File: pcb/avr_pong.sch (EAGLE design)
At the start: 5 parts, among them U1 ATMEGA328P_PDIP, Y1 16 MHz

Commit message: Updated schematic.
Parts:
- added C3, C4: (no value), rcl:CPOL-USE2.5-5
- added IC1: 7805TV, linear:7805TV
- added ICSP: PINHD-2X3THM, adaprog:PINHD-2X3THM
- added J1: DCJ0202, con-jack:DCJ0202
- added LED1: (no value), led:LED5MM
- added R2: 330, rcl:R-US_0207/10
- added R3, R5: 470, rcl:R-US_0207/10
- added R4: 1k, rcl:R-US_0207/10
- added RIGHT, RIGHT1: TACTILE-SWITCH-PTH, GeekAmmo:TACTILE-SWITCH-PTH
- added RV1: (no value), SparkFun-Electromechanical:POT-RV16AF-20
- added S1: (no value), switch:M251
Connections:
- removed net N$3: R1.2, U1.PC6(/RESET)
- removed net VCC: R1.1, U1.VCC
- new net +5V: C4.+, IC1.VO, ICSP.2, R1.1, R2.1, RV1.A, U1.VCC
- new net MISO: ICSP.1, U1.PB4(MISO)
- new net MOSI: ICSP.4, R5.1, U1.PB3(MOSI/OC2)
- new net N$10: R3.1, U1.PD7(AIN1)
- new net N$11: R4.1, U1.PB1(OC1A)
- new net N$12: R3.2
- new net N$13: R4.2
- new net N$4: LED1.A, R2.2
- new net N$5: C3.+, IC1.VI, J1.1
- new net N$6: J1.2, J1.3
- new net N$7: C3.-, S1.P
- new net N$8: RIGHT1.1, U1.PD2(INT0)
- new net N$9: RV1.S, U1.PC0(ADC0)
- new net RST: ICSP.5, R1.2, RIGHT.3, U1.PC6(/RESET)
- new net SCK: ICSP.3, U1.PB5(SCK)
- net GND: now also C4.-, IC1.GND, ICSP.6, LED1.C, RIGHT.1, RIGHT1.3, RV1.E, S1.O
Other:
- moved on the sheet: R1

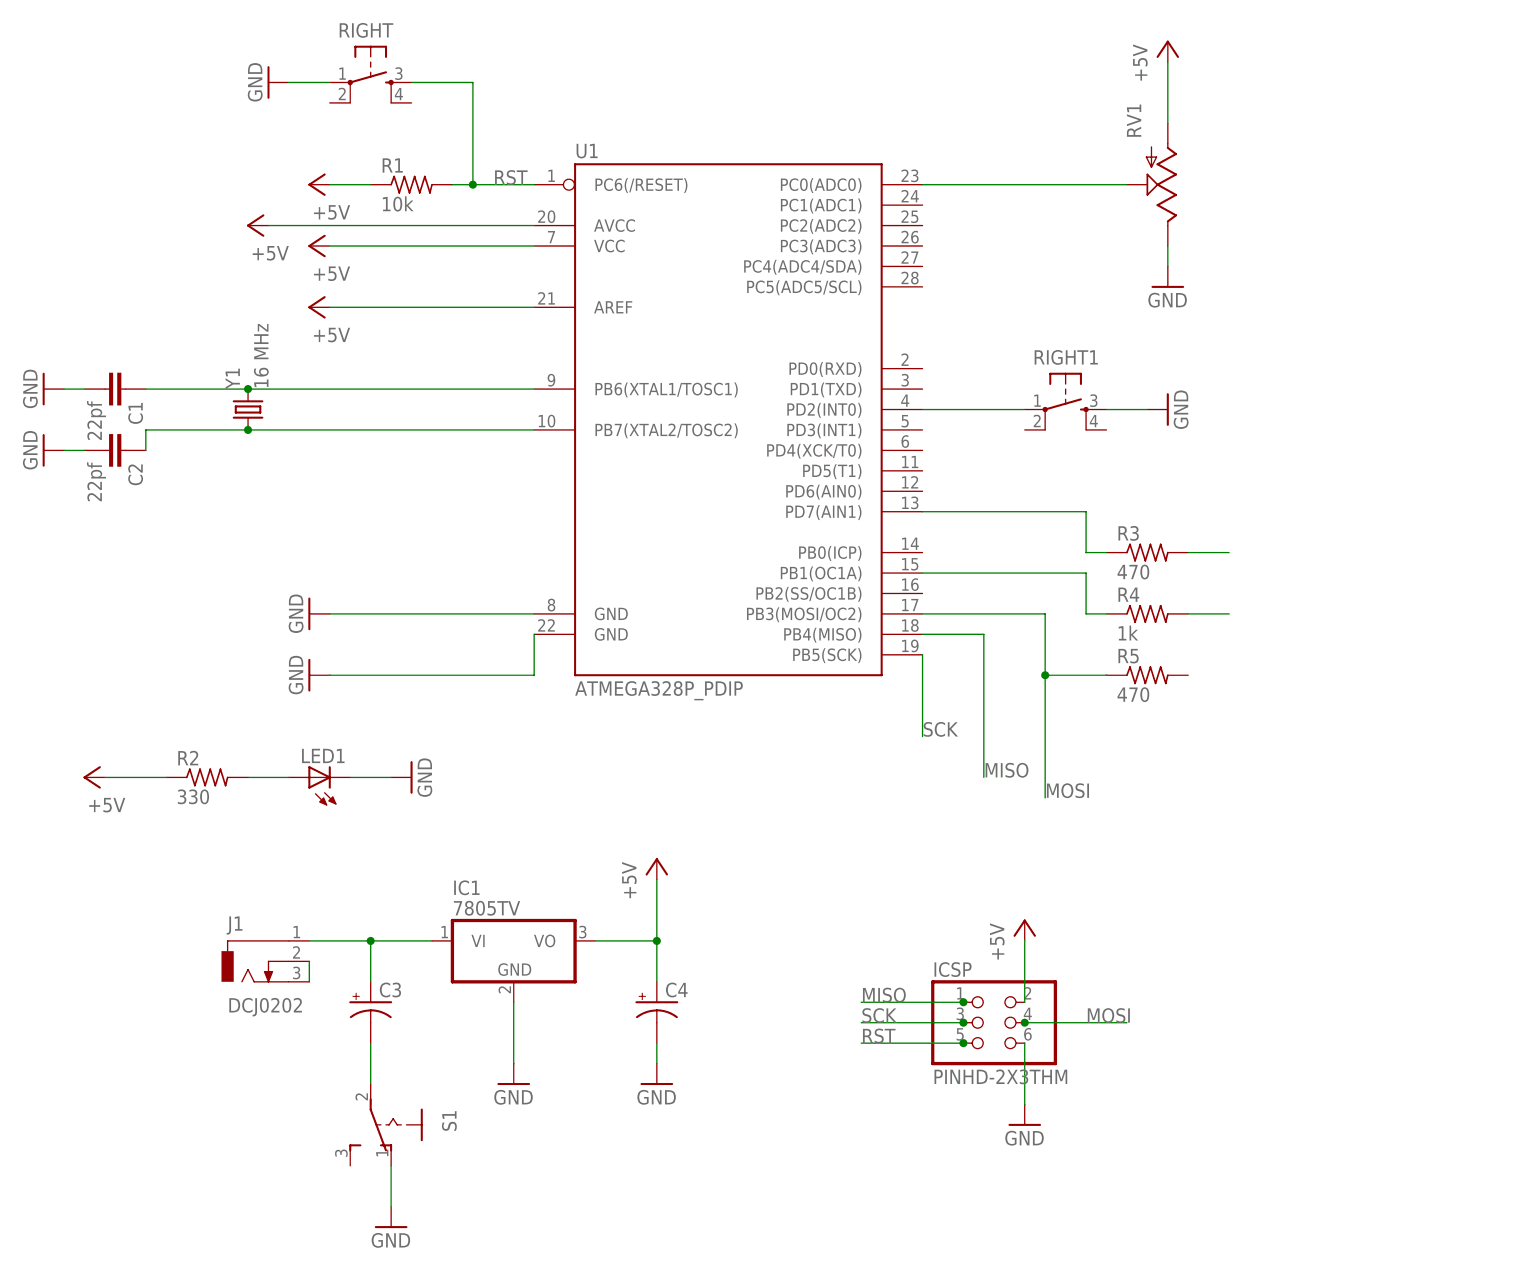
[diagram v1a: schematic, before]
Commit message: Updated schematic and added board layout.
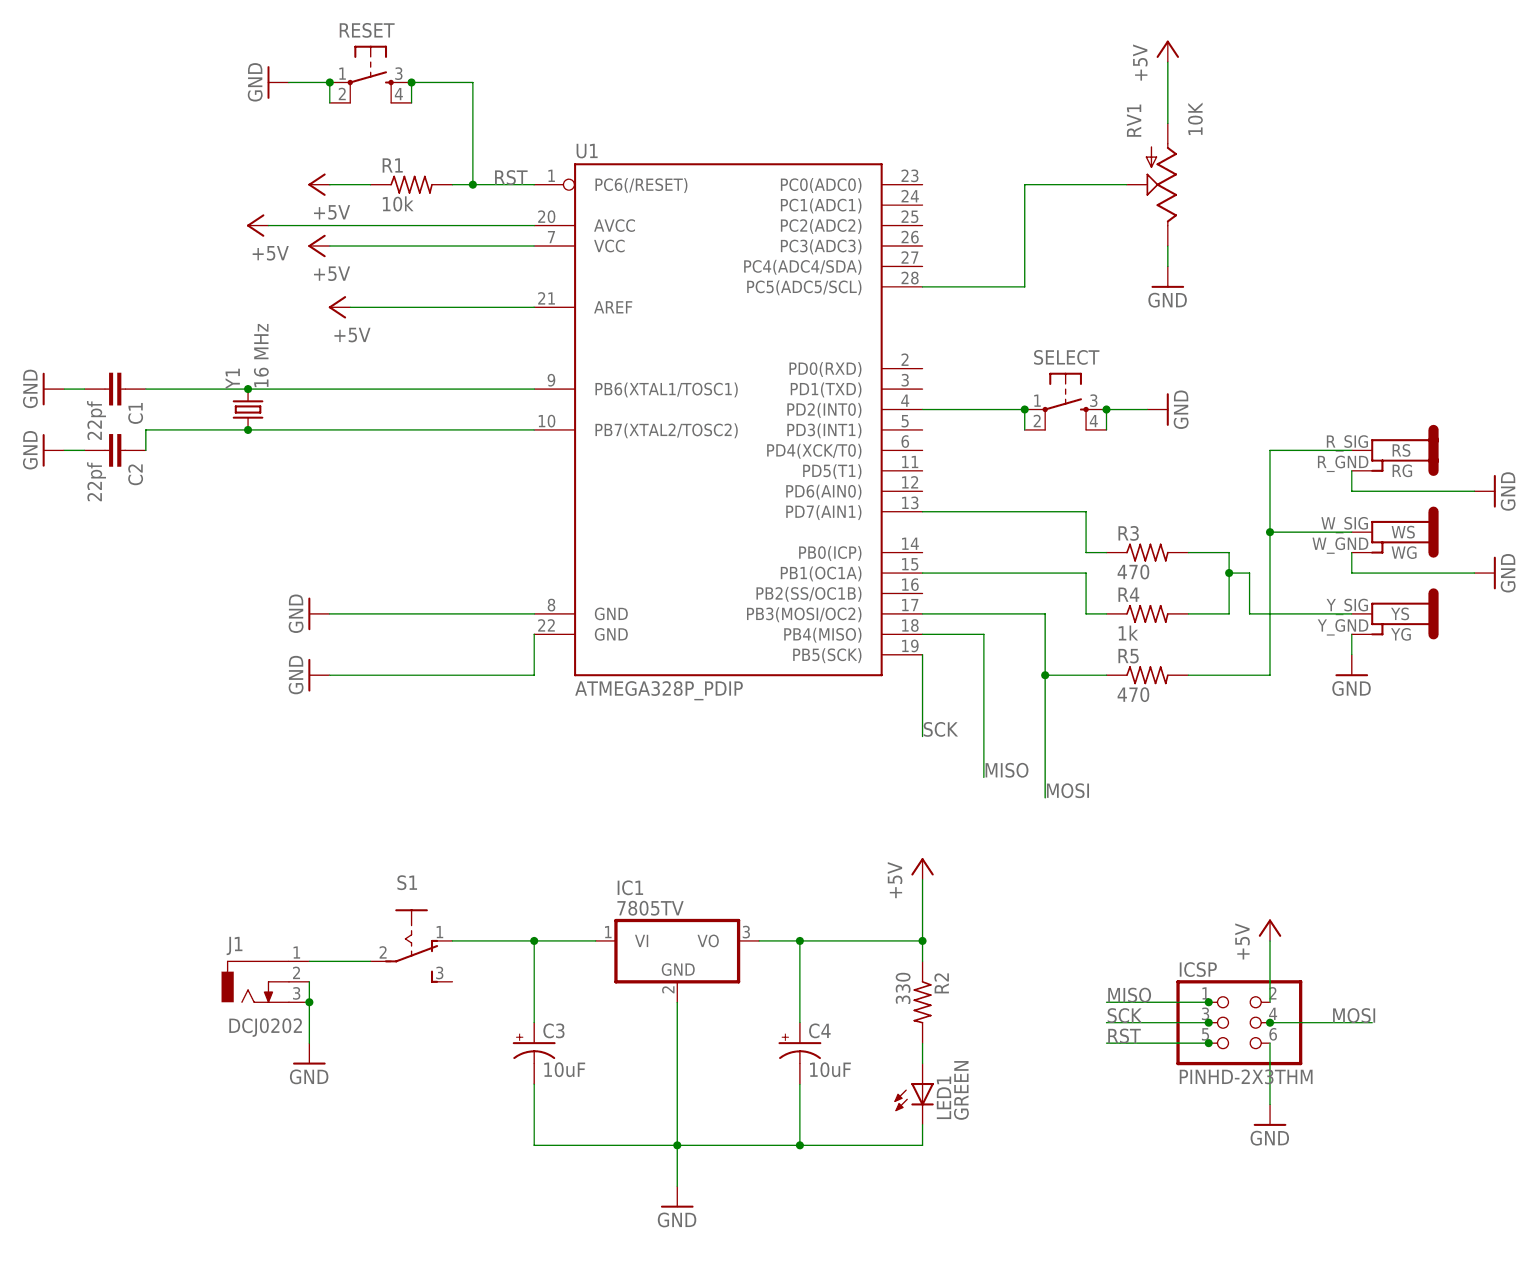
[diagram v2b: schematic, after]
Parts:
- added U$1: 3-RCA-JACK, 3-rca-jack:3-RCA-JACK
- C3, C4: value (none) -> 10uF
- LED1: value (none) -> GREEN
- RV1: value (none) -> 10K
- renumbered RIGHT to RESET, RIGHT1 to SELECT
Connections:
- removed net N$13: R4.2
- removed net N$9: RV1.S, U1.PC0(ADC0)
- new net N$3: R5.2, U$1.RS, U$1.WS
- net +5V: now also U1.AREF, U1.AVCC
- net GND: now also C3.-, J1.2, J1.3, RESET.2, SELECT.4, U$1.RG, U$1.WG, U$1.YG; no longer S1.O
- net N$1: now also U1.PB6(XTAL1/TOSC1)
- net N$12: now also R4.2, U$1.YS
- net N$5: now also S1.O; no longer J1.1
- net N$6: now also J1.1, S1.P; no longer J1.2, J1.3
- net N$7: now also RV1.S, U1.PC5(ADC5/SCL); no longer C3.-, S1.P
- net N$8: now also SELECT.2
- net RST: now also RESET.4
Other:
- moved on the sheet: C3, C4, IC1, ICSP, J1, LED1, R2, S1

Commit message: Added PCB layout.
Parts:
- removed J1: DCJ0202, con-jack:DCJ0202
- added JP1: POWER_JACKPTH, SparkFun-Connectors:POWER_JACKPTH
- S1: value (none) -> Black
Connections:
- net GND: now also JP1.GND, JP1.GNDBREAK; no longer J1.2, J1.3
- net N$6: now also JP1.PWR; no longer J1.1
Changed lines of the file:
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@@
 <part name="ICSP" library="adaprog" deviceset="PINHD-2X3" device="THM"/>
 <part name="GND10" library="supply1" deviceset="GND" device=""/>
-<part name="J1" library="con-jack" deviceset="DCJ0202" device=""/>
 <part name="IC1" library="linear" deviceset="78*" device="TV" technology="05"/>
 <part name="GND5" library="supply1" deviceset="GND" device=""/>
@@
 <part name="RESET" library="GeekAmmo" deviceset="TACTILE-SWITCH" device="-PTH" value=""/>
 <part name="GND11" library="supply1" deviceset="GND" device=""/>
-<part name="S1" library="switch" deviceset="M251" device=""/>
+<part name="S1" library="switch" deviceset="M251" device="" value="Black"/>
 <part name="SELECT" library="GeekAmmo" deviceset="TACTILE-SWITCH" device="-PTH" value=""/>
 <part name="GND8" library="supply1" deviceset="GND" device=""/>
@@
 <part name="GND14" library="supply1" deviceset="GND" device=""/>
 <part name="GND15" library="supply1" deviceset="GND" device=""/>
+<part name="JP1" library="SparkFun-Connectors" deviceset="POWER_JACK" device="PTH"/>
 </parts>
 <sheets>
@@
 <instance part="ICSP" gate="G$1" x="132.08" y="-25.4"/>
 <instance part="GND10" gate="1" x="137.16" y="-38.1"/>
-<instance part="J1" gate="G$1" x="10.16" y="-20.32"/>
 <instance part="IC1" gate="A1" x="63.5" y="-15.24"/>
 <instance part="GND5" gate="1" x="63.5" y="-48.26"/>
-<instance part="GND6" gate="1" x="17.78" y="-30.48"/>
+<instance part="GND6" gate="1" x="12.7" y="-27.94"/>
 <instance part="C3" gate="G$1" x="45.72" y="-27.94"/>
 <instance part="C4" gate="G$1" x="78.74" y="-27.94"/>
@@
 <instance part="GND14" gate="1" x="165.1" y="30.48" rot="R90"/>
 <instance part="GND15" gate="1" x="147.32" y="17.78"/>
+<instance part="JP1" gate="G$1" x="10.16" y="-25.4"/>
 </instances>
 <busses>
@@
 </segment>
 <segment>
-<pinref part="J1" gate="G$1" pin="2"/>
-<pinref part="J1" gate="G$1" pin="3"/>
-<wire x1="17.78" y1="-20.32" x2="17.78" y2="-22.86" width="0.1524" layer="91"/>
+<pinref part="JP1" gate="G$1" pin="GNDBREAK"/>
+<pinref part="JP1" gate="G$1" pin="GND"/>
+<wire x1="12.7" y1="-20.32" x2="12.7" y2="-22.86" width="0.1524" layer="91"/>
+<wire x1="12.7" y1="-22.86" x2="12.7" y2="-25.4" width="0.1524" layer="91"/>
+<junction x="12.7" y="-22.86"/>
 <pinref part="GND6" gate="1" pin="GND"/>
-<wire x1="17.78" y1="-22.86" x2="17.78" y2="-27.94" width="0.1524" layer="91"/>
-<junction x="17.78" y="-22.86"/>
 </segment>
 </net>
@@
 </segment>
 </net>
-<net name="N$6" class="0">
-<segment>
-<pinref part="J1" gate="G$1" pin="1"/>
-<pinref part="S1" gate="1" pin="P"/>
-<wire x1="17.78" y1="-17.78" x2="25.4" y2="-17.78" width="0.1524" layer="91"/>
-</segment>
-</net>
 <net name="N$1" class="0">
 <segment>
@@
 </segment>
 </net>
+<net name="N$6" class="0">
+<segment>
+<pinref part="S1" gate="1" pin="P"/>
+<pinref part="JP1" gate="G$1" pin="PWR"/>
+<wire x1="25.4" y1="-17.78" x2="12.7" y2="-17.78" width="0.1524" layer="91"/>
+</segment>
+</net>
